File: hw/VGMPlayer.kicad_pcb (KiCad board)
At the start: 4 copper layers, 40 x 67 mm, 95 parts, among them J1 Micro_SD_Card, J2 EarPiece, P1 USB_C_Receptacle_16P, P2 SWD, P3 BATT, P5 ICSP, P6 CODEC, Q1 AO3401A, Q2 AO3401A, Q3 2N7002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

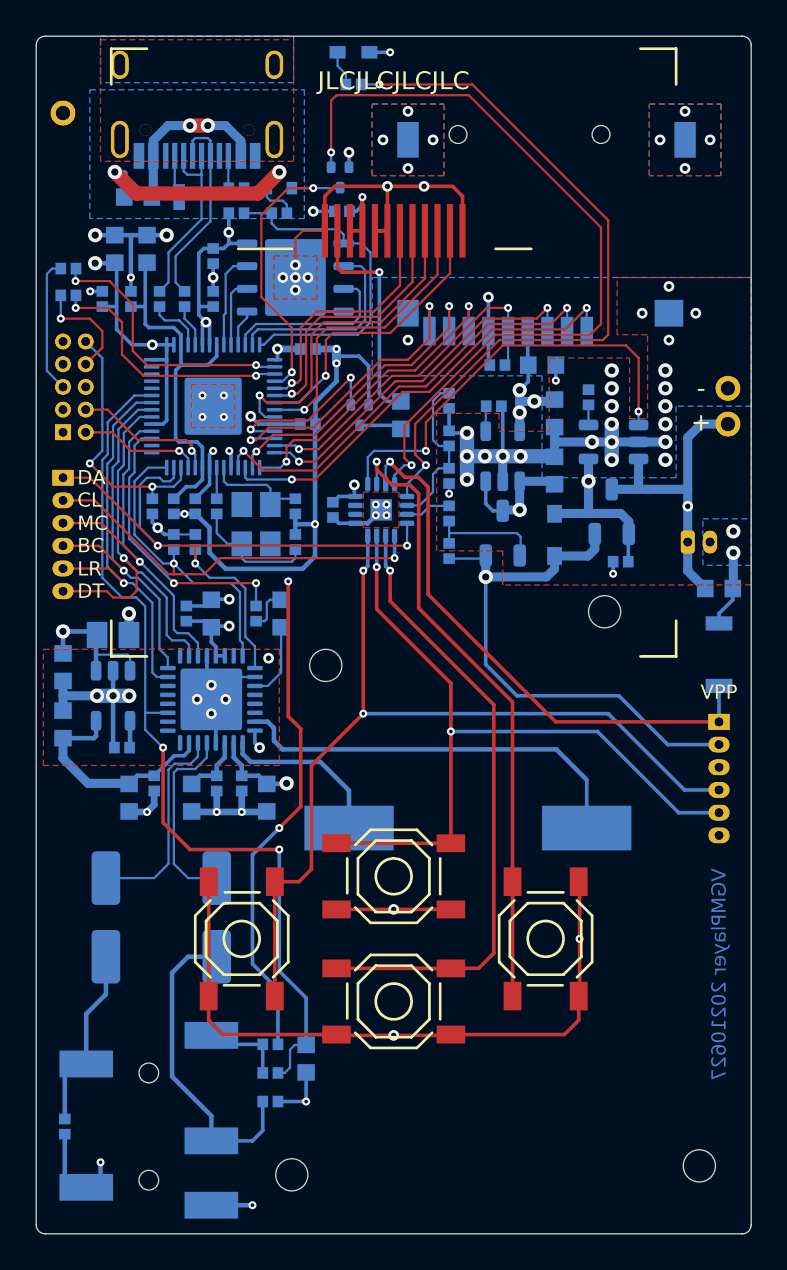
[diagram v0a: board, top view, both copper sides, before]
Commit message: Remove SD card bypass capacitor (very close to main filter cap)
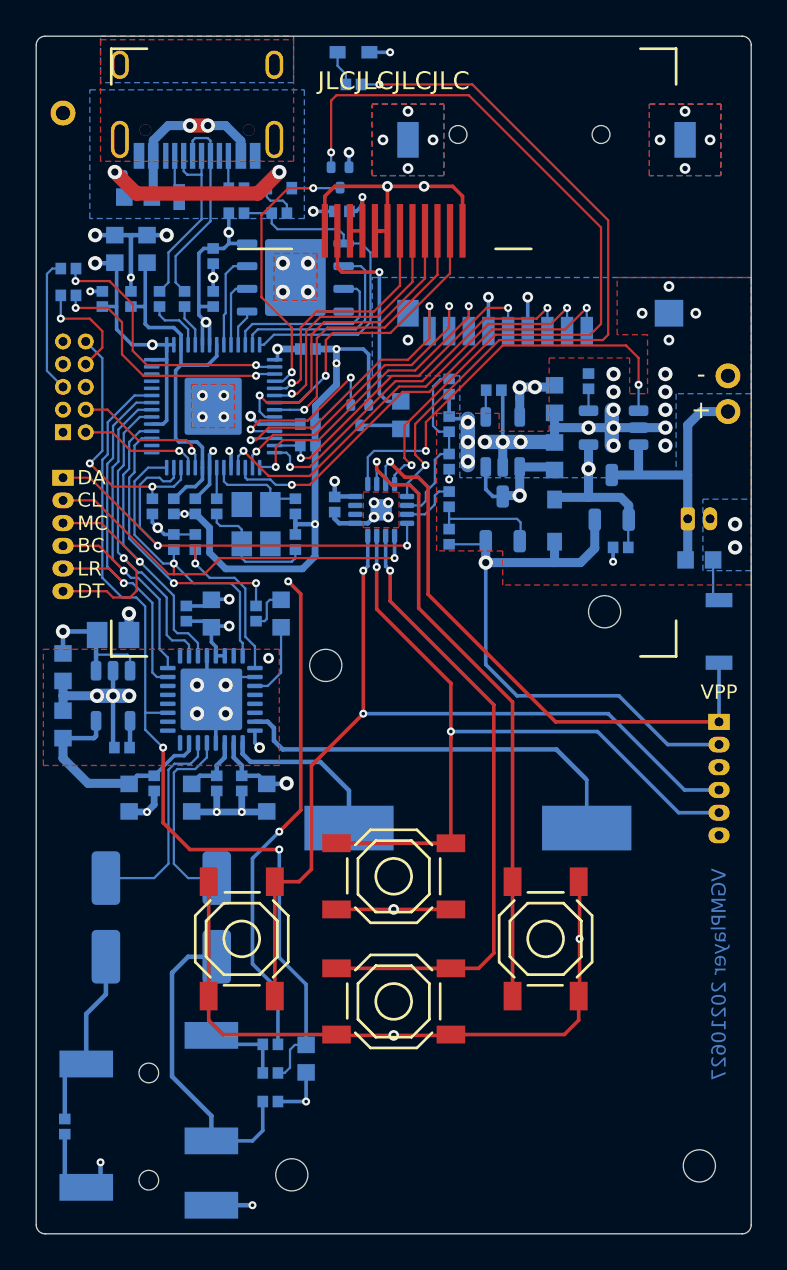
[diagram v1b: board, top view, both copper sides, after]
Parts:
- removed C15: 10u, BZ_Capacitor:C_0603
- moved R11 11.5 mm to (145.2, 99.9), turned to 0 degrees
- moved C31 1.94 mm to (167.1, 106.3)
- moved P3 1.30 mm to (166.4, 104.0)
- moved S5 1.30 mm to (168.2, 110.3)
- moved C34 0.90 mm to (155.6, 96.8)
- moved R18 0.90 mm to (160.9, 96.3)
- moved C36 0.80 mm to (153.1, 96.6)
- moved D2 0.80 mm to (159.0, 104.1)
- moved R19 0.80 mm to (162.7, 105.6)
- moved C33 0.80 mm to (159.0, 100.5)
- moved C35 0.80 mm to (159.0, 97.3)
- moved Q1 0.80 mm to (162.2, 102.8)
- moved Q2 0.80 mm to (156.1, 104.0)
- moved R20 0.80 mm to (153.1, 105.0)
- moved R21 0.80 mm to (153.1, 102.9)
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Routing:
- net 3V3: track 131.8 -> 92.8 mm
- net GND: track 199.7 -> 190.6 mm, vias 86 -> 82
- net VRAW: track 43.8 -> 45.7 mm
- net /VPP: track 31.3 -> 32.6 mm
- net /SD_CLK: track 19.7 -> 18.4 mm
- net Net-(U5-Pad1): track 24.2 -> 23.3 mm
- net VIN: track 36.9 -> 37.7 mm
- net Net-(C36-Pad1): track 9.31 -> 10.1 mm
- net VUSB: track 61.6 -> 60.9 mm
- net Net-(R21-Pad2): track 2.50 -> 3.17 mm
- net /BATT: track 31.5 -> 30.9 mm, vias 2 -> 1
- net /SD_CMD: track 20.5 -> 21.1 mm

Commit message: Initial commit of EC code
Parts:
- moved P2 5.24 mm to (132.8, 94.1), turned to 270 degrees
- moved R25 1.50 mm to (131.8, 91.5)
- moved R26 1.50 mm to (131.8, 90.0)
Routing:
- net /SWCLK: track 8.08 -> 18.4 mm
- net /SWDIO: track 6.85 -> 14.9 mm
- net /RUN: track 14.7 -> 9.84 mm, vias 2 -> 1
- net Net-(P2-Pad8): track 6.15 -> 8.94 mm, vias 1 -> 0
- net /RX: track 14.5 -> 16.4 mm
- net /TX: track 15.3 -> 14.1 mm

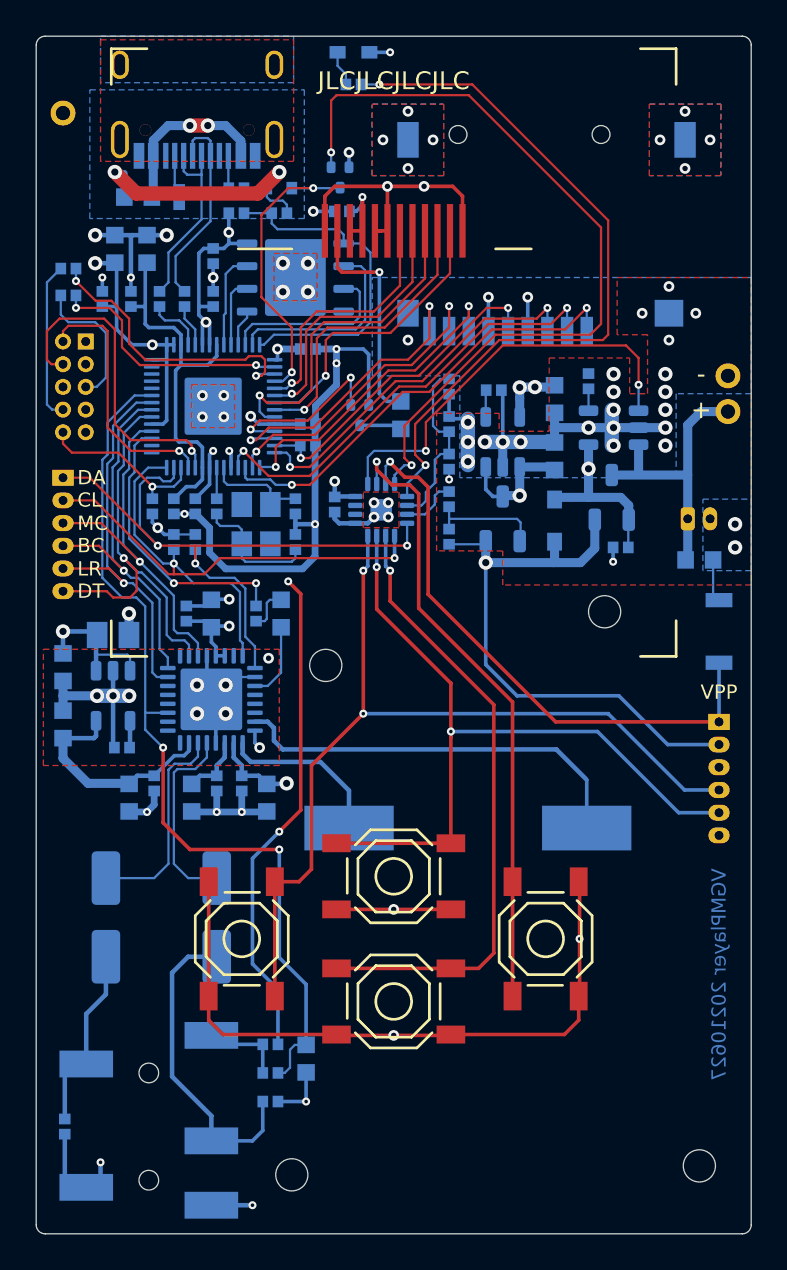
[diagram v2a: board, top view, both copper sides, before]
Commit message: Add analog power selection jumper and multiple button options
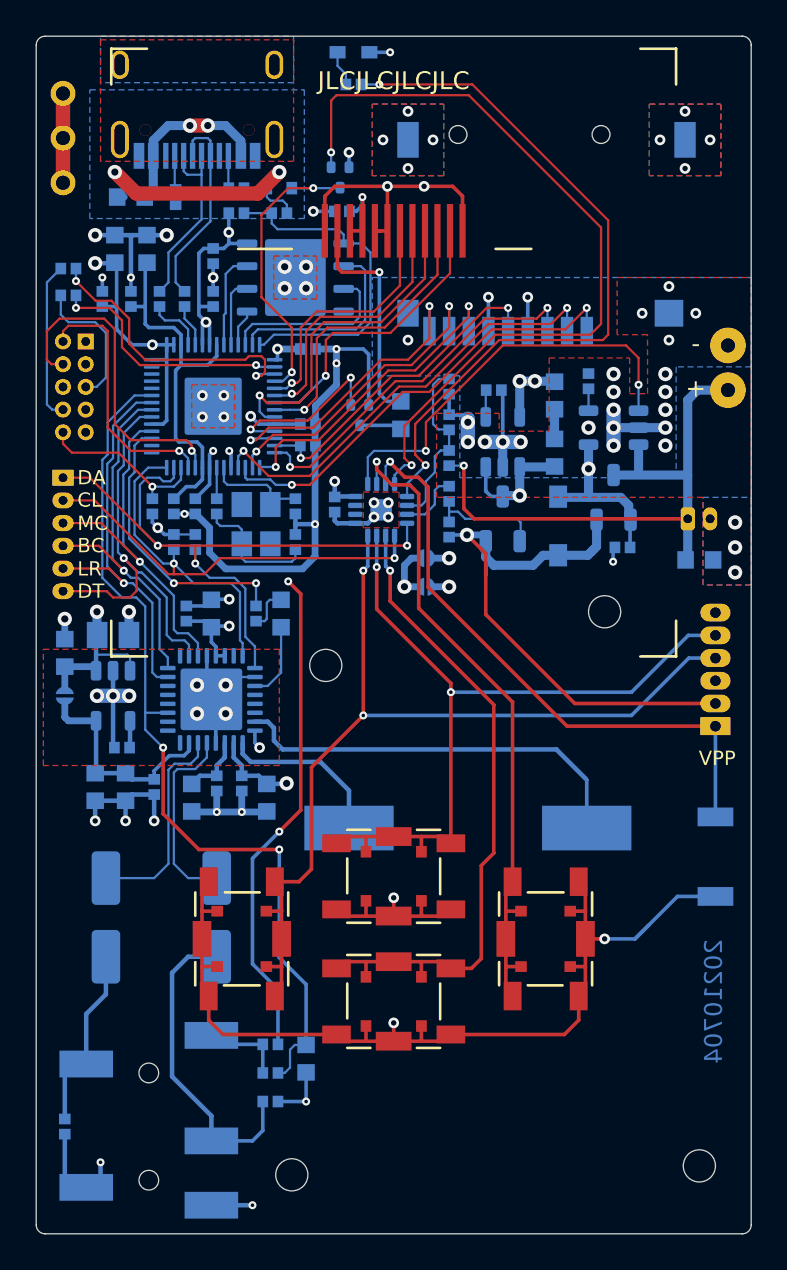
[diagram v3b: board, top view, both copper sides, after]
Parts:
- added JP1: Jumper-NC, BZ_Misc:Jumper-Solder, B.Cu at (151.8, 106.2)
- added JP2: Jumper-NO, BZ_Misc:Jumper-Solder, B.Cu at (151.8, 107.8)
- added JP3: Jumper-NO, BZ_Misc:Jumper-Solder, B.Cu at (131.6, 113.9)
- added TP3: TP, BZ_Misc:TP_THT-Pad-0.8, B.Cu at (131.5, 80.2)
- added TP4: TP, BZ_Misc:TP_THT-Pad-0.8, B.Cu at (131.5, 82.7)
- D2: value B0540WS -> 1N5819HW; footprint BZ_Diode:D_SOD-323 -> BZ_Diode:D_SOD-123
- R19: value 10K -> 100K
- S1, S2, S3, S4: footprint BZ_Switch:C&K_PTS525 -> VGMPlayer:MultiButton
- S5: footprint BZ_Switch:SW-PUSH_3x2x0.6H -> BZ_Switch:SW-PUSH_4x3x2H
- moved S5 12.6 mm to (168.0, 122.9), turned to 90 degrees
- moved C25 3.94 mm to (133.3, 119.0), turned to 270 degrees
- moved TP5 3.90 mm to (131.5, 85.2)
- moved TP2 1.70 mm to (168.7, 94.3)
- moved TP1 1.20 mm to (168.7, 96.8)
- moved C23 0.81 mm to (131.6, 111.5), turned to 90 degrees
- moved C20 0.63 mm to (135.0, 119.0)
- moved R20 0.40 mm to (153.1, 104.6)
- moved C2 0.40 mm to (135.3, 86.0)
- moved D2 0.36 mm to (159.2, 104.4)
- moved P5 0.31 mm to (168.0, 115.6), turned to 90 degrees
- moved R21 0.30 mm to (153.1, 102.6)
- moved C19 0.20 mm to (136.6, 119.0)
- moved C33 0.20 mm to (159.0, 100.3)
- moved C35 0.20 mm to (159.0, 97.1)
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- renumbered TP3 to TP1, TP1 to TP5
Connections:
- C33 pad 1: VIN -> Net-(C33-Pad1)
- Q2 pad 3: VIN -> Net-(C33-Pad1)
- U7 pad 1: VIN -> Net-(C33-Pad1)
- U7 pad 3: VIN -> Net-(C33-Pad1)
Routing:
- net GND: track 190.6 -> 212.6 mm, vias 82 -> 84
- net 3V3: track 92.8 -> 109.7 mm, vias 15 -> 16
- net Net-(C33-Pad1): track 0.00 -> 14.7 mm, vias 0 -> 2
- net VIN: track 37.7 -> 23.6 mm
- net /BATT: track 30.9 -> 33.3 mm
- net Net-(S2-Pad2): track 34.9 -> 36.9 mm
- net Net-(S4-Pad2): track 35.0 -> 36.8 mm
- net VUSB: track 60.9 -> 62.5 mm
- net /VPP: track 32.6 -> 34.1 mm
- net /ICSPDAT: track 50.4 -> 51.8 mm
- net /ICSPCLK: track 42.2 -> 43.5 mm
- net VRAW: track 45.7 -> 44.7 mm
- net VDDA: track 13.1 -> 12.4 mm
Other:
- board text added: "20210704"
- board text removed: "VGMPlayer 20210627"

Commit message: more pcb editing
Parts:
- moved C25 3.36 mm to (131.6, 116.1)
- moved C23 0.20 mm to (131.6, 111.7)
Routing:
- net GND: track 212.6 -> 209.5 mm, vias 84 -> 82
- net 3V3: track 109.7 -> 110.0 mm, vias 16 -> 15

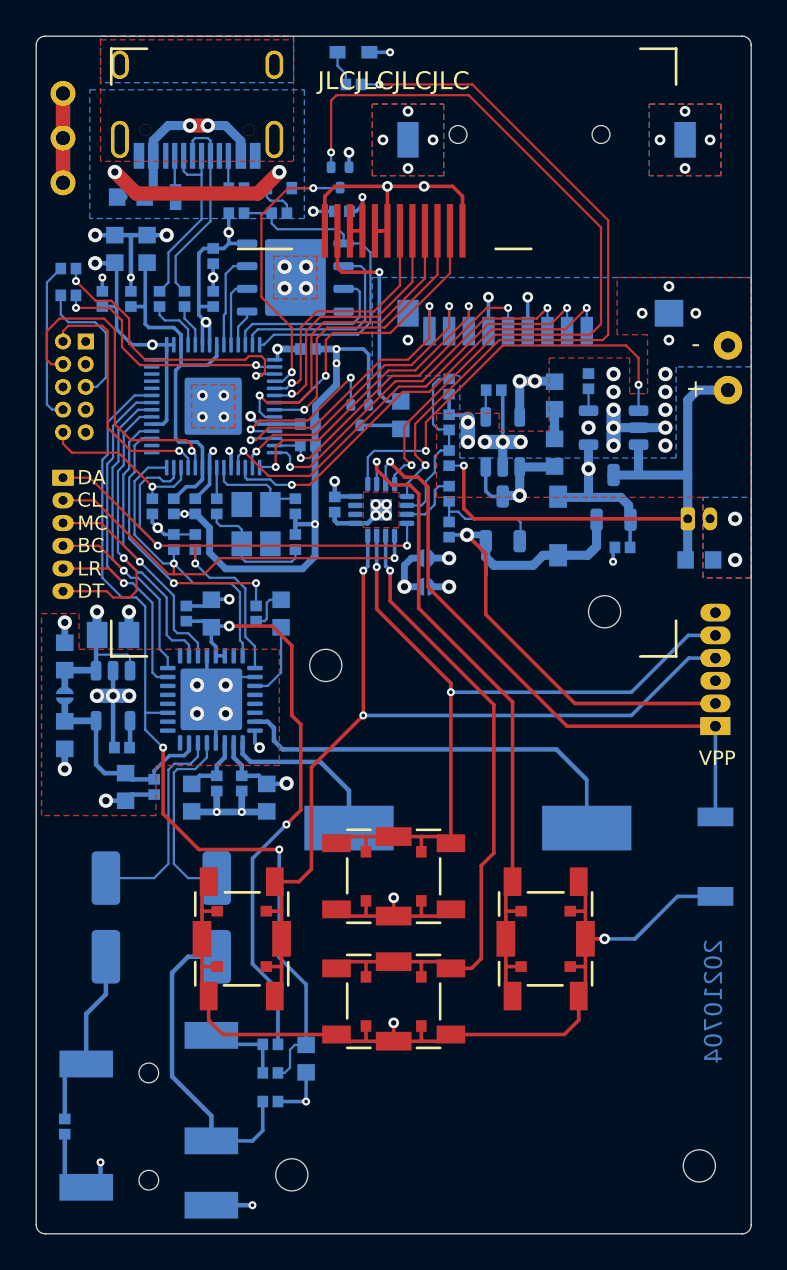
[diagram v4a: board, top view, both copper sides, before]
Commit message: Fix LCD wiring
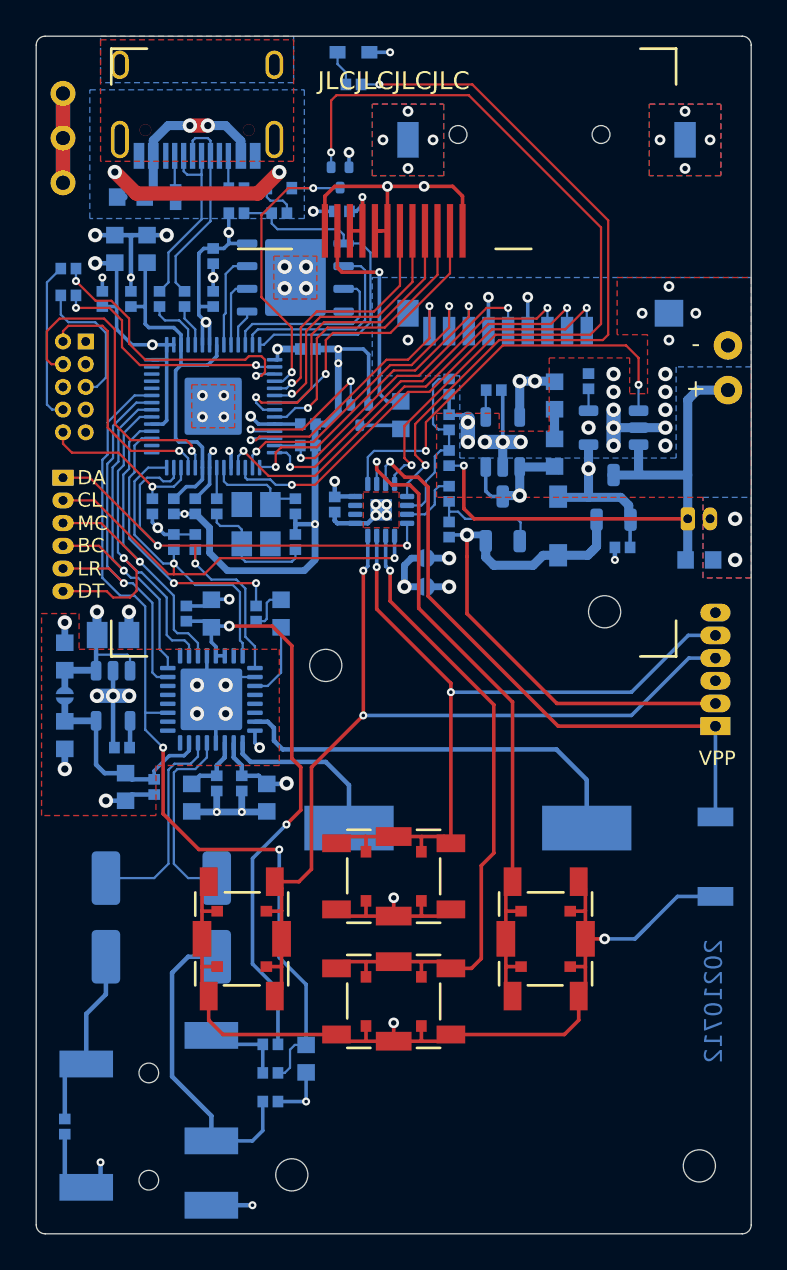
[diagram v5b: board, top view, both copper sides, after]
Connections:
- DISP1 pad 10: /SCLK -> /MOSI
- DISP1 pad 9: /MOSI -> /SCLK
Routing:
- net /MOSI: track 18.6 -> 16.9 mm
- net /SCLK: track 16.6 -> 18.4 mm
- net GND: track 209.5 -> 210.1 mm
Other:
- board text added: "20210712"
- board text removed: "20210704"

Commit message: Further layout optimize
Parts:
- moved R10 0.22 mm to (137.9, 105.4)
- moved R9 0.22 mm to (139.1, 105.4)
- moved C6 0.20 mm to (137.9, 103.3)
- moved R7 0.20 mm to (140.3, 103.3)
- moved C11 0.20 mm to (139.1, 103.3)
- moved C3 0.20 mm to (144.7, 103.3)
- moved C4 0.20 mm to (144.7, 105.3)
- moved R6 0.20 mm to (136.7, 103.3)
- moved Y1 0.20 mm to (142.5, 104.3)
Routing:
- net GND: track 210.1 -> 212.7 mm, vias 82 -> 85
- net /SCL: track 39.3 -> 38.2 mm
- net /JACK_DET: track 49.9 -> 50.6 mm
- net /I2S_LRC: track 22.7 -> 23.3 mm
- net 3V3: track 110.0 -> 109.5 mm
- net Net-(R22-Pad1): track 41.0 -> 41.5 mm
- added copper zone on B.Cu, net 3V3
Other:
- board text added: "20210714"
- board text removed: "20210712"
